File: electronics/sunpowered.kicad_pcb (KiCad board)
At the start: 2 copper layers, 90.2 x 59.7 mm, 19 parts, among them IC1 ACS713, P1 CONN_01X02, P2 CONN_02X04, P3 CONN_01X02, Q1 PSMN0R9-30YLD, T1 12A

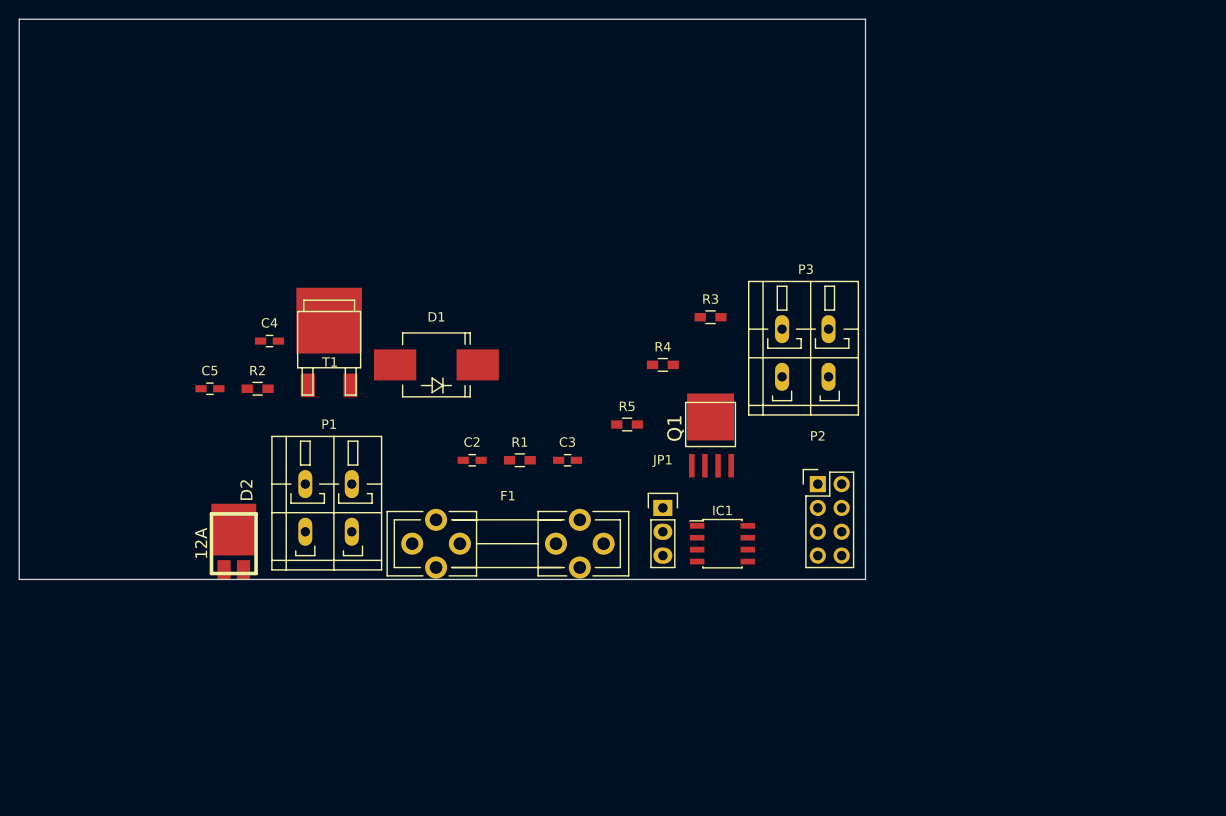
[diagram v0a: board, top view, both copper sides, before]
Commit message: input baord: initial component placement
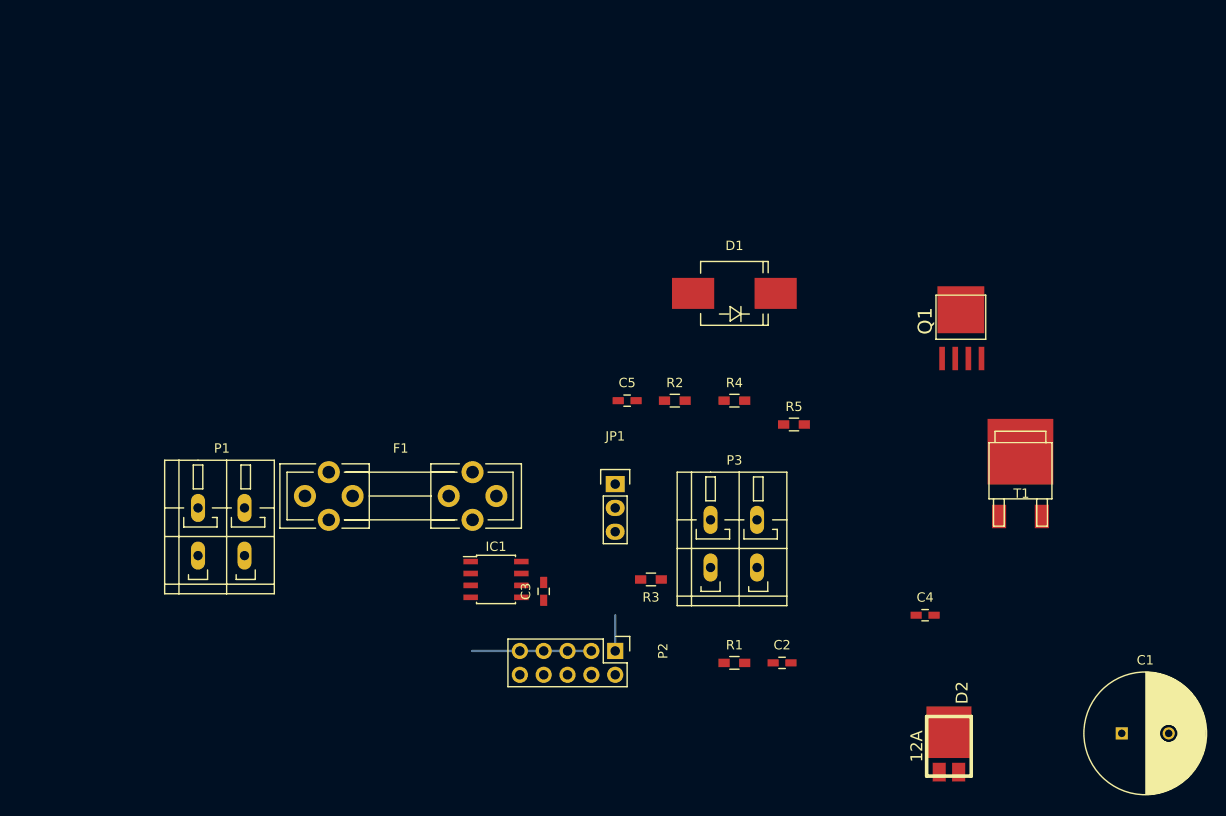
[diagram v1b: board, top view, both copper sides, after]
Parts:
- added C1: 4700u, Capacitors_ThroughHole:C_Radial_D13_L25_P5, F.Cu at (196.2, 126.9)
- P2: value CONN_02X04 -> CONN_02X05; footprint Pin_Headers:Pin_Header_Straight_2x04 -> Pin_Headers:Pin_Header_Straight_2x05
- moved D2 79.2 mm to (177.8, 128.3)
- moved C4 75.7 mm to (175.3, 114.3)
- moved T1 75.0 mm to (185.4, 100.3)
- moved R2 44.5 mm to (148.6, 91.4)
- moved C5 44.5 mm to (143.5, 91.4)
- moved C2 39.5 mm to (160.0, 119.4)
- moved D1 32.7 mm to (154.9, 80.0)
- moved R1 31.4 mm to (154.9, 119.4)
- moved Q1 29.0 mm to (179.1, 82.5)
- moved R3 28.7 mm to (146.1, 110.5), turned to 180 degrees
- moved P2 28.0 mm to (142.2, 118.1), turned to 270 degrees
- moved IC1 24.4 mm to (129.5, 110.5)
- moved P3 21.7 mm to (154.9, 106.7)
- moved R5 17.8 mm to (161.3, 94.0)
- moved C3 14.2 mm to (134.6, 111.8), turned to 90 degrees
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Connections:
- C2 pad 2: GNDD -> Net-(C2-Pad2)
- C3 pad 1: GNDD -> DigitalGround
- D1 pad 1: Net-(C5-Pad1) -> Net-(C4-Pad1)
- D1 pad 2: Net-(C4-Pad1) -> Net-(C5-Pad1)
- IC1 pad 5: GNDD -> DigitalGround
- P2 pad 1: PanelVoltageSense+ -> Net-(P2-Pad1)
- P2 pad 2: GNDD -> +5V
- P2 pad 3: PanelVoltageSense- -> DigitalGround
- P2 pad 4: CurrentSensorVoltageSense -> PanelVoltageSense+
- P2 pad 5: PowerOn -> DigitalGround
- P2 pad 6: +5V -> CurrentSensorVoltageSense
- P2 pad 7: PanelCurrentSense -> DigitalGround
- P2 pad 8: GNDD -> PanelCurrentSense
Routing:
- net DigitalGround: track 0.00 -> 12.7 mm
- net Net-(P2-Pad1): track 0.00 -> 3.81 mm
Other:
- board outline removed

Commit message: Upgrade to the newest KiCad version + better caps.
Some of the component symbols got lost while upgrading to the newest KiCad,
recreated them.
Calculated better filter cap values.
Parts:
- C1: value 4700u -> 10u
- Q1: value PSMN0R9-30YLD -> Q_NMOS_SGD
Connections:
- C1 pad 1: +5V -> Net-(C1-Pad1)
- C1 pad 2: DigitalGround -> PanelVoltageSense-
- D2 pad 1: Net-(C4-Pad1) -> Net-(D2-Pad1)
- D2 pad 2: Net-(D2-Pad2) -> Net-(C4-Pad1)
- P2 pad 1: Net-(P2-Pad1) -> PowerOn
- P3 pad 1: Net-(D2-Pad2) -> Net-(D2-Pad1)
- Q1 pad D: Net-(P3-Pad2) -> (no net)
- Q1 pad G: Net-(Q1-PadG) -> (no net)
- Q1 pad S: PanelVoltageSense- -> (no net)
- R3 pad 1: Net-(D2-Pad2) -> Net-(D2-Pad1)
- R5 pad 1: Net-(Q1-PadG) -> Net-(C1-Pad1)
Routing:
- net PowerOn: track 0.00 -> 3.81 mm
- net Net-(P2-Pad1): track 3.81 -> 0.00 mm

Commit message: corrected footprints for diodes
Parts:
- removed C1: 10u, Capacitors_ThroughHole:C_Radial_D13_L25_P5
- removed C2, C4: 100n, Capacitors_SMD:C_0603_HandSoldering
- removed C3, C5: 47n, Capacitors_SMD:C_0603_HandSoldering
- removed D1: 24V, Diodes_SMD:Diode-SMC_Handsoldering
- removed D2: 12A, cyplo's:TO277A
- removed F1: 8A, Fuse_Holders_and_Fuses:Fuseholder5x20_horiz_open_universal_Type-III
- removed IC1: ACS713, Housings_SOIC:SOIC-8_3.9x4.9mm_Pitch1.27mm
- removed JP1: JUMPER3, Pin_Headers:Pin_Header_Straight_1x03
- removed P1, P3: CONN_01X02, Terminal_Blocks:TerminalBlock_WAGO-236_2Stift_RM5mm_2pol
- removed P2: CONN_02X05, Pin_Headers:Pin_Header_Straight_2x05
- removed Q1: Q_NMOS_SGD, cyplo's:LFPAK56
- removed R1: 330, Resistors_SMD:R_0603_HandSoldering
- removed R2, R5: 1k, Resistors_SMD:R_0603_HandSoldering
- removed R3: 5k, Resistors_SMD:R_0603_HandSoldering
- removed R4: 10k, Resistors_SMD:R_0603_HandSoldering
- removed T1: 12A, cyplo's:sot428
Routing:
- net DigitalGround: track 12.7 -> 0.00 mm
- net PowerOn: track 3.81 -> 0.00 mm

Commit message: overvoltage detector layout
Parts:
- added C1: 100n, Capacitors_SMD:C_1206_HandSoldering, F.Cu at (123.4, 119.6)
- added C2: 47n, Capacitors_SMD:C_0805_HandSoldering, F.Cu at (136.4, 120.4)
- added C3: 47n, Capacitors_SMD:C_1206_HandSoldering, F.Cu at (138.4, 110.0)
- added C4: 10u, Capacitors_SMD:C_1206_HandSoldering, F.Cu at (161.0, 109.5)
- added D1: 12A, TO SOT SMD:TO-252-2Lead, F.Cu at (119.4, 111.8)
- added D2: 22V, Diodes SMD:SMB_Standard, F.Cu at (132.6, 115.8)
- added F1: 8A, Fuse_Holders_and_Fuses:Fuseholder5x20_horiz_open_universal_Type-III, F.Cu at (116.3, 101.1)
- added P1: CONN_01X04, ab2_terminal_block:AB2_TB_04_RA_5MM_L-GRN, F.Cu at (108.7, 117.3)
- added P2: CONN_01X04, ab2_terminal_block:AB2_TB_04_RA_5MM_R-GRN, F.Cu at (176.3, 115.8)
- added P3: CONN_01X04, Pin Headers:Pin_Header_Straight_1x04, F.Cu at (123.4, 126.0)
- added Q1: IRFR13N20D, TO SOT SMD:TO-252-2Lead, F.Cu at (150.9, 127.0)
- added Q2: IRFR13N20D, TO SOT SMD:TO-252-2Lead, F.Cu at (161.0, 123.4)
- added R1: 0.01, 1W, Resistors_SMD:R_1206_HandSoldering, F.Cu at (117.3, 122.4)
- added R2: 1k, Resistors_SMD:R_1206_HandSoldering, F.Cu at (128.5, 119.9)
- added R3: 10k, Resistors_SMD:R_1206_HandSoldering, F.Cu at (145.3, 113.0)
- added R4: 1k, Resistors_SMD:R_1206_HandSoldering, F.Cu at (160.8, 127.8)
- added U1: BSL316C, TO SOT SMD:TSOT-6-MK06A_Handsoldering, F.Cu at (132.8, 126.0)
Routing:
- net /Input Measurement And Protection/PanelVoltageSense+: track 0.00 -> 25.6 mm
- net /Input Measurement And Protection/Overvoltage: track 0.00 -> 8.40 mm
- net /Input Measurement And Protection/PanelCurrentSenseHigh: track 0.00 -> 7.06 mm, vias 0 -> 1
- net /Input Measurement And Protection/RawPositive: track 0.00 -> 6.82 mm
- net /Input Measurement And Protection/PanelCurrentSenseLow: track 0.00 -> 2.54 mm
- added copper zone on B.Cu, net /Input Measurement And Protection/PanelCurrentSenseLow
- added copper zone on F.Cu, net /Input Measurement And Protection/PanelCurrentSenseLow
- added copper zone on B.Cu, net /Input Measurement And Protection/PanelVoltageSense+
- added copper zone on F.Cu, net /Input Measurement And Protection/RawPositive
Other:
- board outline added: 79.8 x 33.8 mm

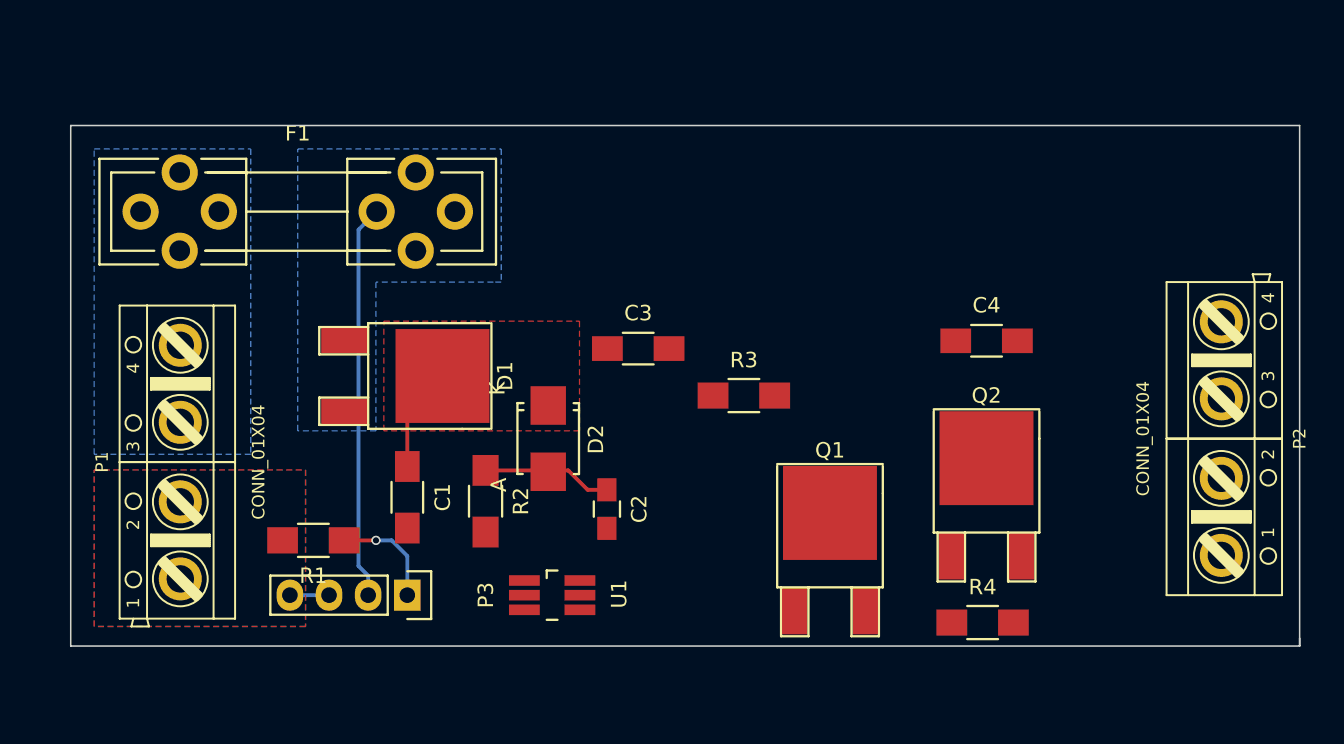
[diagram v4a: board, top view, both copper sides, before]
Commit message: basic layout for the input board
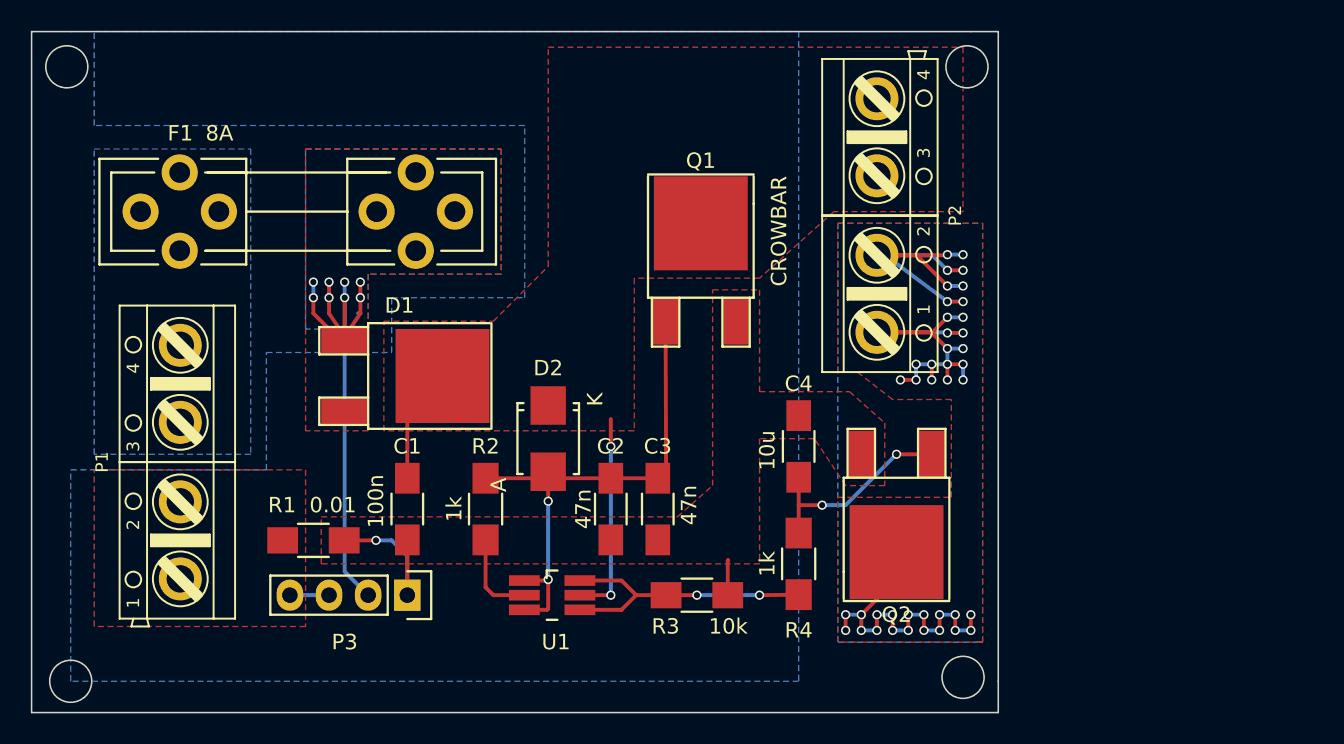
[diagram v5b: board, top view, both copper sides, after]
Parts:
- C2: footprint Capacitors_SMD:C_0805_HandSoldering -> Capacitors_SMD:C_1206_HandSoldering
- Q1: value IRFR13N20D -> CROWBAR
- R1: value 0.01, 1W -> 0.01
- moved P2 26.6 mm to (153.9, 101.3)
- moved Q1 20.6 mm to (142.5, 108.2)
- moved C4 14.0 mm to (148.8, 116.3), turned to 90 degrees
- moved R3 13.3 mm to (142.2, 126.0)
- moved R4 12.5 mm to (148.8, 124.0), turned to 270 degrees
- moved C3 10.5 mm to (139.7, 120.4), turned to 270 degrees
- moved Q2 8.82 mm to (155.2, 116.8), turned to 180 degrees
- moved C1 0.76 mm to (123.4, 120.4)
- moved R2 0.51 mm to (128.5, 120.4)
- moved C2 0.25 mm to (136.7, 120.4)
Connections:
- P2 pad 1: /Input Measurement And Protection/RawPositive -> /Input Measurement And Protection/RawGround
- P2 pad 2: /Input Measurement And Protection/RawPositive -> /Input Measurement And Protection/RawGround
- P2 pad 3: /Input Measurement And Protection/RawGround -> /Input Measurement And Protection/RawPositive
- P2 pad 4: /Input Measurement And Protection/RawGround -> /Input Measurement And Protection/RawPositive
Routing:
- net /Input Measurement And Protection/RawGround: track 0.00 -> 73.6 mm, vias 0 -> 41
- net /Input Measurement And Protection/Overvoltage: track 8.40 -> 34.2 mm, vias 0 -> 2
- net /Input Measurement And Protection/VoltageOK: track 0.00 -> 18.6 mm, vias 0 -> 2
- net /Input Measurement And Protection/RawPositive: track 6.82 -> 21.0 mm, vias 0 -> 2
- net Net-(C4-Pad1): track 0.00 -> 13.6 mm, vias 0 -> 2
- net /Input Measurement And Protection/PanelCurrentSenseHigh: track 7.06 -> 19.5 mm
- net /Input Measurement And Protection/PanelVoltageSense+: track 25.6 -> 37.3 mm, vias 0 -> 8
- added copper zone on F.Cu, net /Input Measurement And Protection/PanelCurrentSenseHigh
- added copper zone on F.Cu, net /Input Measurement And Protection/PanelVoltageSense+
- added copper zone on B.Cu, net /Input Measurement And Protection/RawGround
- added copper zone on F.Cu, net /Input Measurement And Protection/RawGround
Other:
- board size 79.8 x 33.8 mm -> 62.7 x 44.2 mm

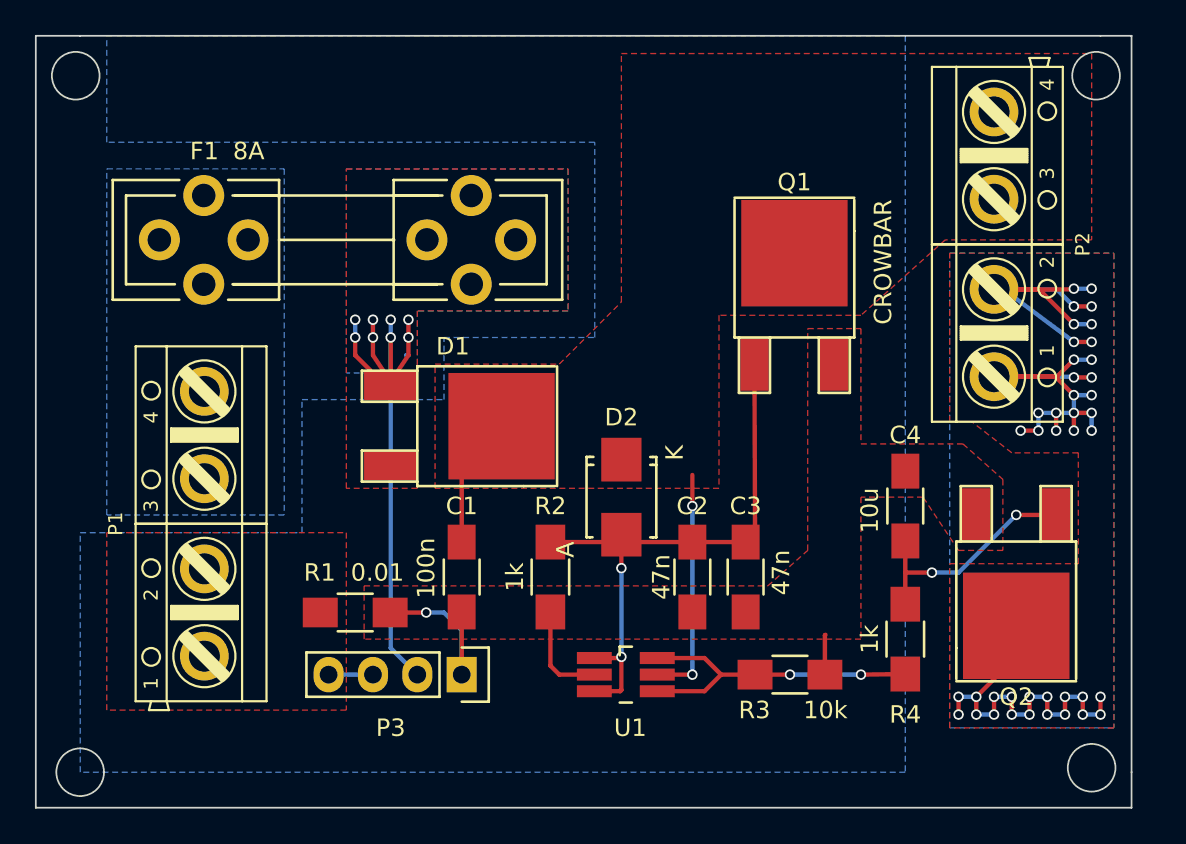
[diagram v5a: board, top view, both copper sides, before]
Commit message: annotations on the board
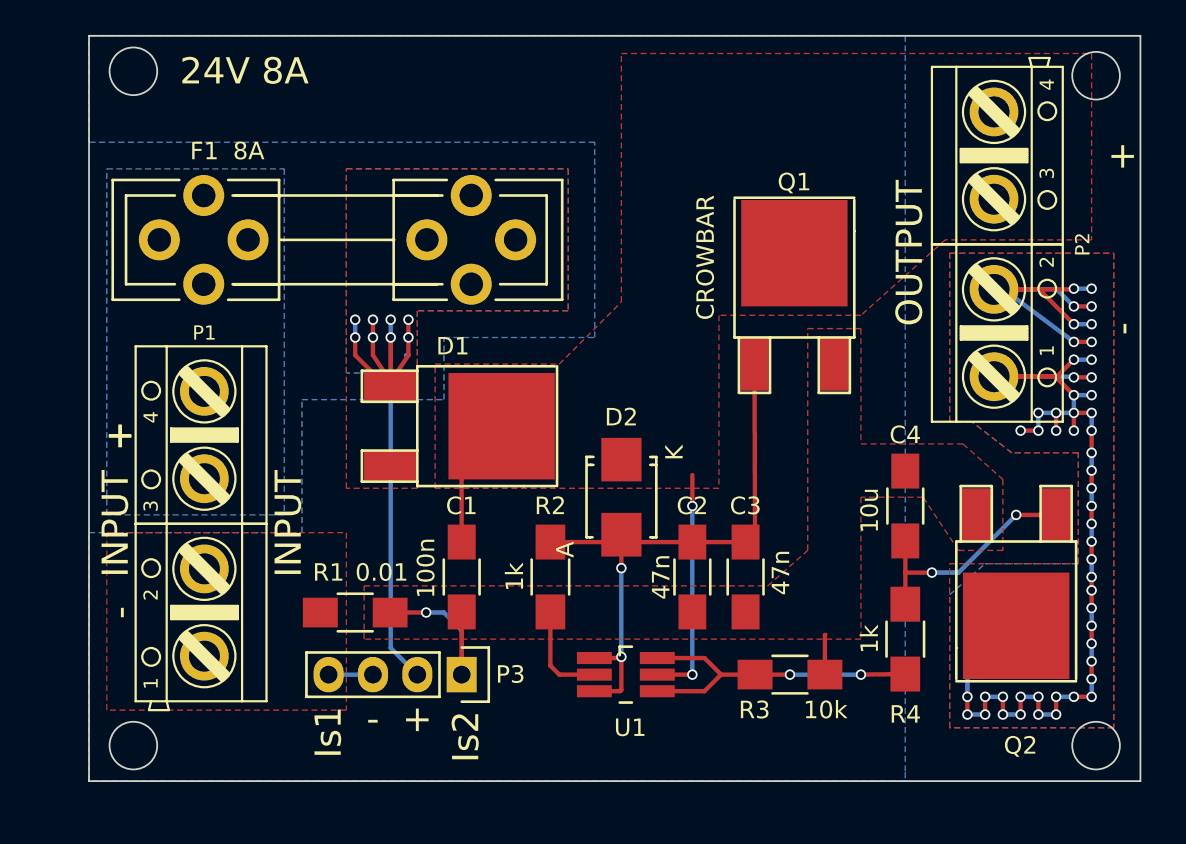
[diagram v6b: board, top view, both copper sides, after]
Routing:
- net /Input Measurement And Protection/RawGround: track 73.6 -> 83.1 mm, vias 41 -> 51
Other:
- board size 62.7 x 44.2 mm -> 60.2 x 42.7 mm
- board text added: "+"
- board text added: "-"
- board text added: "24V 8A"
- board text added: "INPUT"
- board text added: "Is1"
- board text added: "Is2"
- board text added: "OUTPUT"

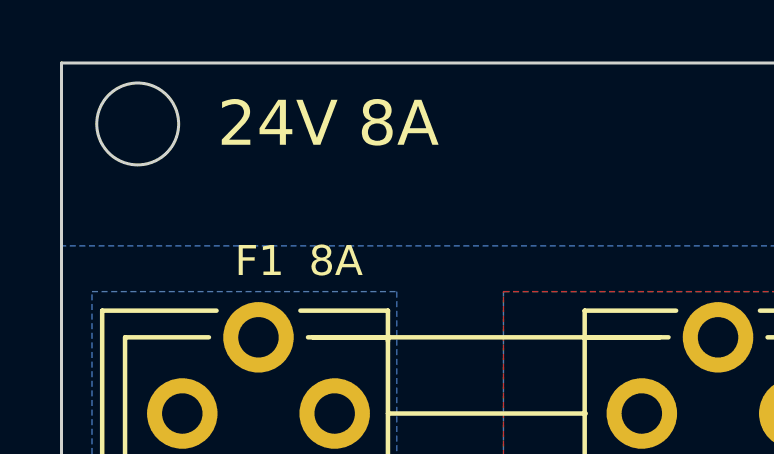
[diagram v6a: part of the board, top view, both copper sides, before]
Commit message: input board designators
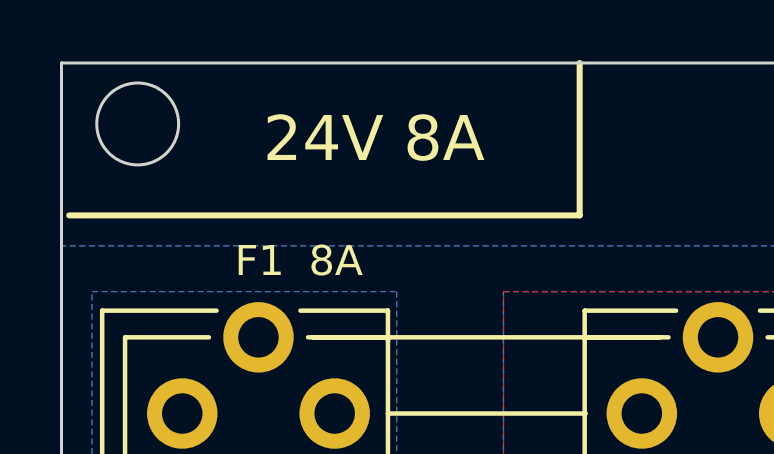
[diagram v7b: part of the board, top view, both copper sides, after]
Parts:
- added REF**: Symbol_OSHW-Logo_SilkScreen_BIG, Symbols:Symbol_OSHW-Logo_SilkScreen_BIG, B.Cu at (140.2, 124.2)
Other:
- board text added: "24V 8A, rev A 2015-12, cyplo@cyplo.net"
- board text added: "Sunpowered Input Protection and Measurement Board https://lab.cyplo.net/cyplo/sunpowered"

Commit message: more vias for power planes
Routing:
- net /Input Measurement And Protection/PanelVoltageSense+: track 37.3 -> 59.3 mm, vias 8 -> 24
- net /Input Measurement And Protection/Overvoltage: track 34.2 -> 42.6 mm
